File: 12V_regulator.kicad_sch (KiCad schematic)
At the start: 17 parts

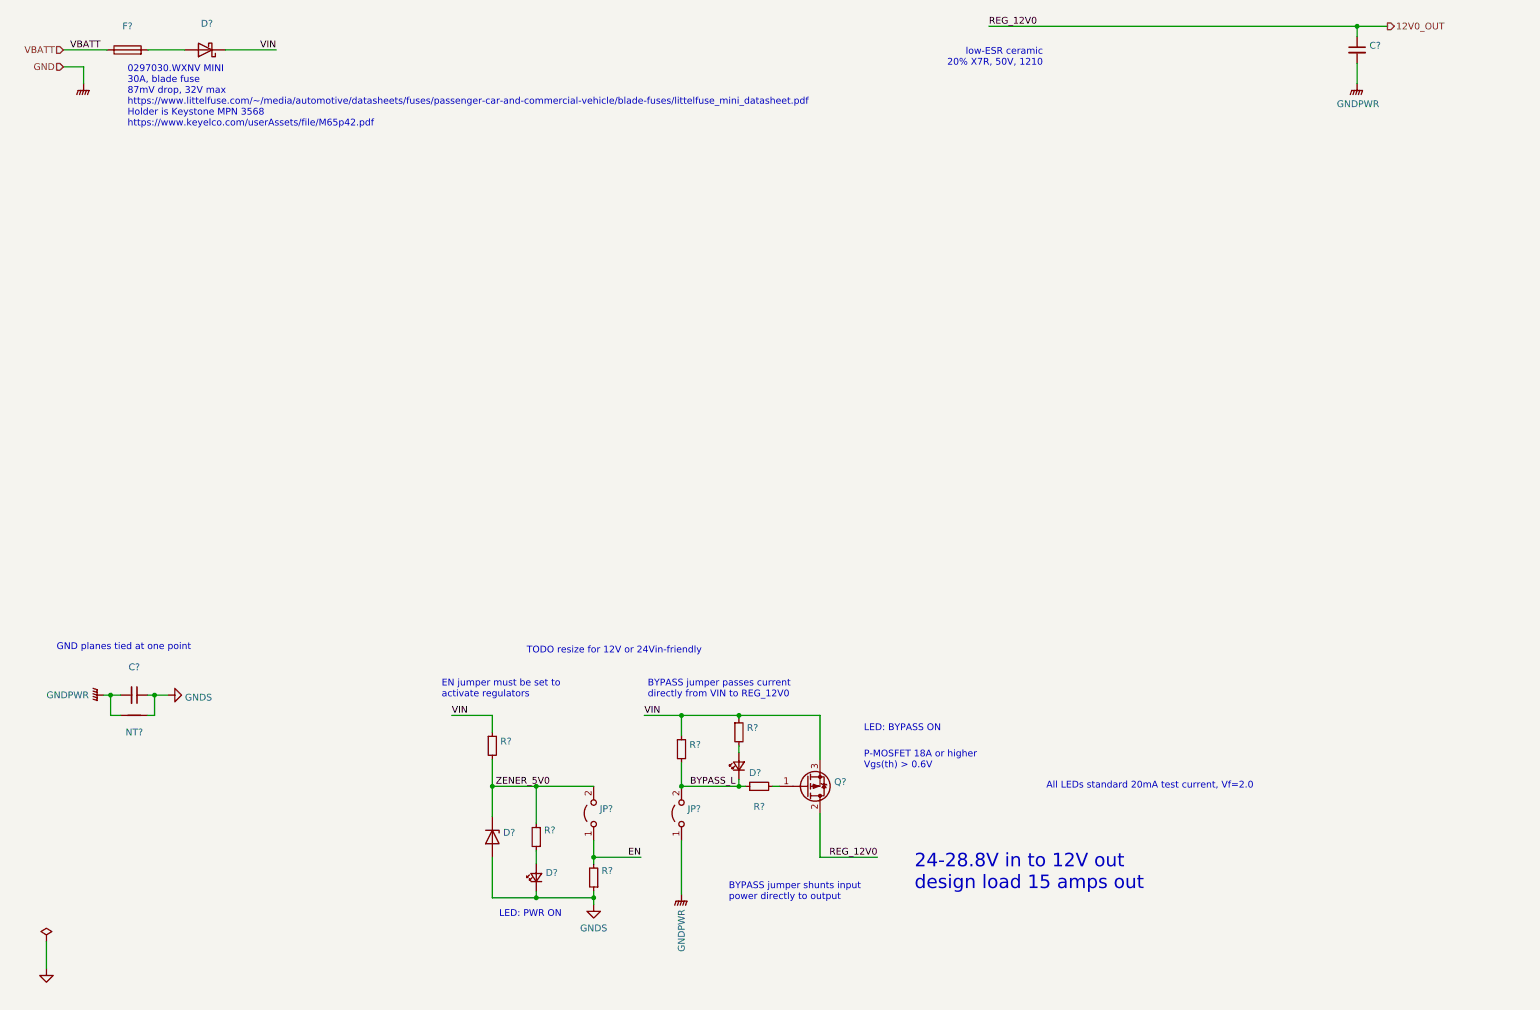
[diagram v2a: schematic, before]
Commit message: Sketch out ISL8117-driven 12V regulator.
Another candidate entry for on-board 12V regulation is to
build our own based on the reference schematic from the ISL8117
DC buck regulator controller datasheet.

Implemented (most of) this reference schematic here.
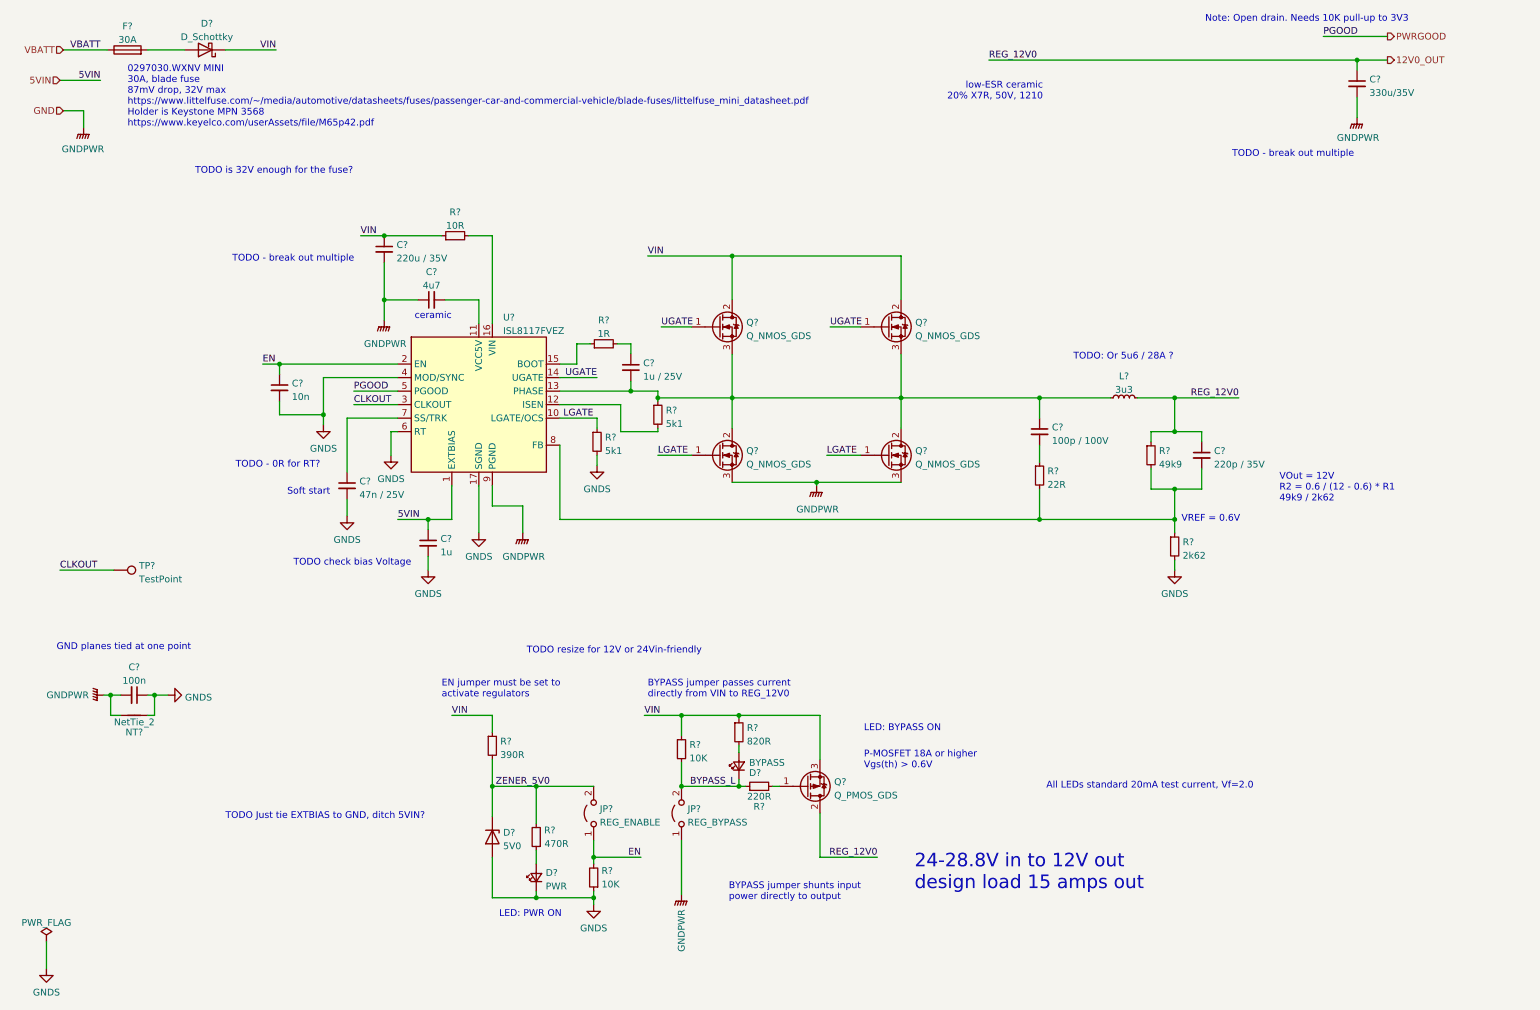
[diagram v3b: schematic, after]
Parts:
- added C?: 1u, symbol Device:C_Small
- added C?: 4u7, symbol Device:C_Small
- added C?: 1u / 25V, symbol Device:C_Small
- added C?: 10n, symbol Device:C_Small
- added C?: 100p / 100V, symbol Device:C_Small
- added C?: 220u / 35V, symbol Device:C_Small
- added C?: 47n / 25V, symbol Device:C_Small
- added C?: 220p / 35V, symbol Device:C_Small
- added L?: 3u3, symbol Device:L_Small
- added Q? (x4): Q_NMOS_GDS, symbol Device:Q_NMOS_GDS
- added R?: 22R, symbol Device:R_Small
- added R?: 49k9, symbol Device:R_Small
- added R?: 2k62, symbol Device:R_Small
- added R?: 10R, symbol Device:R_Small
- added R? (x2): 5k1, symbol Device:R_Small
- added R?: 1R, symbol Device:R_Small
- added TP?: TestPoint, symbol Connector:TestPoint
- added U?: ISL8117FVEZ, Package_SO:HTSSOP-16-1EP_4.4x5mm_P0.65mm_EP3.4x5mm, symbol Regulator_Switching:ISL8117FVEZ
- C?: value (none) -> 100n
- C?: value (none) -> 330u/35V; footprint (none) -> Capacitor_SMD:C_1210_3225Metric
- D?: value (none) -> 5V0
- D?: value (none) -> PWR
- D?: value (none) -> BYPASS
- D?: value (none) -> D_Schottky
- F?: value (none) -> 30A
- JP?: value (none) -> REG_BYPASS
- JP?: value (none) -> REG_ENABLE
- NT?: value (none) -> NetTie_2
- Q?: value (none) -> Q_PMOS_GDS
- R?: value (none) -> 220R
- R?: value (none) -> 390R
- R? (x2): value (none) -> 10K
- R?: value (none) -> 470R
- R?: value (none) -> 820R
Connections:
- net 12V0_OUT: now also C?.1, L?.2, R?.1
- net EN: now also C?.1, U?.2 (EN)
- net GNDPWR: now also C?.1, C?.2, Q?.3 (S), Q?.3 (S), U?.9 (PGND)
- net GNDS: now also C?.2, C?.2, C?.2, R?.2, R?.2, U?.17 (SGND), U?.4 (MOD/SYNC), U?.6 (RT)
- net VIN: now also C?.1, Q?.2 (D), Q?.2 (D), R?.1
- new net: C?.2, R?.1
- new net: C?.2, R?.1, R?.2, R?.2, U?.8 (FB)
- new net: C?.1, C?.2, L?.1, Q?.2 (D), Q?.2 (D), Q?.3 (S), Q?.3 (S), R?.1, U?.13 (PHASE)
- new net: C?.2, U?.11 (VCC5V)
- new net: C?.1, R?.2
- new net: R?.2, U?.16 (VIN)
- new net: R?.2, U?.12 (ISEN)
- new net: R?.1, U?.15 (BOOT)
- new net: C?.1, U?.7 (SS/TRK)
- new net 5VIN: C?.1, U?.1 (EXTBIAS)
- new net CLKOUT: TP?.1, U?.3 (CLKOUT)
- new net LGATE: Q?.1 (G), Q?.1 (G), R?.1, U?.10 (LGATE/OCS)
- new net PWRGOOD: U?.5 (PGOOD)
- new net UGATE: Q?.1 (G), Q?.1 (G), U?.14 (UGATE)
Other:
- note added: "Note: Open drain. Needs 10K pull-up to 3V3"
- note added: "Soft start"
- note added: "TODO - 0R for RT?"
- note added: "TODO - break out multiple"
- note added: "TODO Just tie EXTBIAS to GND, ditch 5VIN?"
- note added: "TODO check bias Voltage"
- note added: "TODO is 32V enough for the fuse?"
- note added: "TODO: Or 5u6 / 28A ?"
- note added: "VOut = 12V R2 = 0.6 / (12 - 0.6) * R1 49k9 / 2k62"
- note added: "VREF = 0.6V"
- note added: "ceramic"
- moved on the sheet: C?
